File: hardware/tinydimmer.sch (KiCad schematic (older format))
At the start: 37 parts, among them J1 CTB7000/6, J2 CTB7000/2, Q1 IRL540N, SW1 SW_Push, T1 Hahn EL 305 2051, U1 BAJ0CC0T, U2 Digispark USB, U3 Busch_Dimmer_2112U_101

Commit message: Adjust pads, rewire connectors, change footprints
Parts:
- added H5: MountingHole_Pad, MountingHole:MountingHole_3.2mm_M3_Pad, symbol Mechanical:MountingHole_Pad
- D5: footprint Diode_THT:D_DO-35_SOD27_P7.62mm_Horizontal -> Diode_THT:D_DO-35_SOD27_P3.81mm_Vertical_AnodeUp
- R2, R3: footprint Resistor_THT:R_Axial_DIN0207_L6.3mm_D2.5mm_P10.16mm_Horizontal -> Resistor_THT:R_Axial_DIN0207_L6.3mm_D2.5mm_P5.08mm_Vertical
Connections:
- net GND: now also J1.3 (Pin_3), H5.1; no longer J1.5 (Pin_5)
- net PWM: now also R2.1; no longer R2.2
- net SW_NEG: now also J1.5 (Pin_5); no longer J1.1 (Pin_1)
- net SW_POS: now also J1.1 (Pin_1); no longer J1.3 (Pin_3)
- net at Q1.1 (G), R3.1: now also R2.2; no longer R2.1
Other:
- note added: "Load ground"
- note added: "Load positive"
- note added: "Potentiometer negative"
- note added: "Potentiometer positive"
- note added: "Supply ground"
- note added: "Supply positive"
- note removed: "To LED PSU"
- note removed: "To LEDs"
- note removed: "To potentiometer"
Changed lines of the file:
@@
 F 0 "R2" V 3993 4175 50  0000 C CNN
 F 1 "1K" V 4084 4175 50  0000 C CNN
-F 2 "Resistor_THT:R_Axial_DIN0207_L6.3mm_D2.5mm_P10.16mm_Horizontal" V 4130 4175 50  0001 C CNN
+F 2 "Resistor_THT:R_Axial_DIN0207_L6.3mm_D2.5mm_P5.08mm_Vertical" V 4130 4175 50  0001 C CNN
 F 3 "~" H 4200 4175 50  0001 C CNN
 	1    4200 4175
-	0    1    1    0
+	0    -1   -1   0
 $EndComp
 $Comp
@@
 F 0 "R3" H 4520 4471 50  0000 L CNN
 F 1 "10K" H 4520 4380 50  0000 L CNN
-F 2 "Resistor_THT:R_Axial_DIN0207_L6.3mm_D2.5mm_P10.16mm_Horizontal" V 4380 4425 50  0001 C CNN
+F 2 "Resistor_THT:R_Axial_DIN0207_L6.3mm_D2.5mm_P5.08mm_Vertical" V 4380 4425 50  0001 C CNN
 F 3 "~" H 4450 4425 50  0001 C CNN
 	1    4450 4425
@@
 	0    -1   -1   0
 $EndComp
-Text GLabel 9175 1400 0    50   Input ~ 0
+Text GLabel 9175 1300 0    50   Input ~ 0
 SW_POS
-Text GLabel 9175 1200 0    50   Input ~ 0
+Text GLabel 9175 1600 0    50   Input ~ 0
 SW_NEG
 Text GLabel 9175 1700 0    50   Input ~ 0
 POT_POS
 Wire Wire Line
-	9375 1500 9275 1500
-Wire Wire Line
-	9275 1500 9275 1600
-Wire Wire Line
-	9275 1600 9375 1600
-Wire Wire Line
 	9375 1400 9275 1400
 Wire Wire Line
+	9275 1400 9275 1500
+Wire Wire Line
+	9275 1500 9375 1500
+Wire Wire Line
 	9375 1300 9275 1300
 Wire Wire Line
-	9275 1300 9275 1400
-Connection ~ 9275 1400
-Wire Wire Line
-	9275 1400 9175 1400
-Wire Wire Line
-	9375 1200 9175 1200
+	9375 1200 9275 1200
+Wire Wire Line
+	9275 1200 9275 1300
+Connection ~ 9275 1300
+Wire Wire Line
+	9275 1300 9175 1300
+Wire Wire Line
+	9375 1600 9175 1600
 Wire Wire Line
 	9375 1700 9175 1700
@@
 $EndComp
 Wire Wire Line
-	9275 1850 9275 1600
-Connection ~ 9275 1600
+	9275 1850 9275 1500
+Connection ~ 9275 1500
 Wire Wire Line
 	5250 6050 5450 6050
@@
 F 0 "D5" V 4350 6150 50  0000 L CNN
 F 1 "1N5231" V 4450 6000 50  0000 L CNN
-F 2 "Diode_THT:D_DO-35_SOD27_P7.62mm_Horizontal" H 4350 6300 50  0001 C CNN
+F 2 "Diode_THT:D_DO-35_SOD27_P3.81mm_Vertical_AnodeUp" H 4350 6300 50  0001 C CNN
 F 3 "~" H 4350 6300 50  0001 C CNN
 	1    4350 6300
@@
 Wire Notes Line
 	4575 1325 4600 1325
-Text Notes 9725 1725 0    100  ~ 0
-To potentiometer
-Text Notes 9725 1525 0    100  ~ 0
-To LED PSU
-Text Notes 9725 1325 0    100  ~ 0
-To LEDs
 Wire Wire Line
 	5125 3875 4850 3875
@@
 	1    0    0    -1
 $EndComp
-Wire Wire Line
-	10175 2850 10325 2850
 $Comp
 L power:GND #PWR021
 U 1 1 5DDB9F38
-P 10325 2950
-F 0 "#PWR021" H 10325 2700 50  0001 C CNN
-F 1 "GND" H 10330 2777 50  0000 C CNN
-F 2 "" H 10325 2950 50  0001 C CNN
-F 3 "" H 10325 2950 50  0001 C CNN
-	1    10325 2950
-	1    0    0    -1
-$EndComp
-Wire Wire Line
-	10325 2950 10325 2850
-Connection ~ 10325 2850
-Wire Wire Line
-	10325 2850 10475 2850
+P 10475 3000
+F 0 "#PWR021" H 10475 2750 50  0001 C CNN
+F 1 "GND" H 10480 2827 50  0000 C CNN
+F 2 "" H 10475 3000 50  0001 C CNN
+F 3 "" H 10475 3000 50  0001 C CNN
+	1    10475 3000
+	1    0    0    -1
+$EndComp
 Wire Wire Line
 	9275 2275 9375 2275
@@
 Wire Wire Line
 	3300 1750 3300 2200
+$Comp
+L Mechanical:MountingHole_Pad H5
+U 1 1 5DD960E1
+P 10775 2750
+F 0 "H5" H 10875 2753 50  0000 L CNN
+F 1 "MountingHole_Pad" H 10875 2708 50  0001 L CNN
+F 2 "MountingHole:MountingHole_3.2mm_M3_Pad" H 10775 2750 50  0001 C CNN
+F 3 "~" H 10775 2750 50  0001 C CNN
+	1    10775 2750
+	1    0    0    -1
+$EndComp
+Wire Wire Line
+	10475 2850 10475 2925
+Wire Wire Line
+	10775 2850 10775 2925
+Connection ~ 10475 2925
+Wire Wire Line
+	10475 2925 10775 2925
+Wire Wire Line
+	10475 2925 10475 3000
+Text Notes 9700 1750 0    50   ~ 0
+Potentiometer positive
+Text Notes 9700 1550 0    50   ~ 0
+Potentiometer negative
+Text Notes 9700 1650 0    50   ~ 0
+Load ground
+Text Notes 9700 1250 0    50   ~ 0
+Load positive
+Text Notes 9700 1450 0    50   ~ 0
+Supply ground
+Text Notes 9700 1350 0    50   ~ 0
+Supply positive
+Wire Wire Line
+	10175 2850 10175 2925
+Wire Wire Line
+	10175 2925 10475 2925
 $EndSCHEMATC

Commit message: First PCB draft
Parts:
- D5: footprint Diode_THT:D_DO-35_SOD27_P3.81mm_Vertical_AnodeUp -> Diode_THT:D_DO-35_SOD27_P7.62mm_Horizontal
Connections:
- net ENABLE: now also C5.1
- net at D5.1 (K), R6.1, R7.2: no longer C5.1
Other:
- moved on the sheet: C5, R7, R8
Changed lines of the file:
@@
 	5250 6150 5250 6050
 Wire Wire Line
-	5100 6050 5250 6050
-Connection ~ 4650 6550
+	4775 6050 4925 6050
 Wire Wire Line
 	5250 6550 5250 6450
-Wire Wire Line
-	4650 6550 5250 6550
 $Comp
 L Device:R R8
 U 1 1 5DCDCA32
-P 5250 6300
-F 0 "R8" H 5100 6250 50  0000 C CNN
-F 1 "10K" H 5100 6350 50  0000 C CNN
-F 2 "Resistor_THT:R_Axial_DIN0207_L6.3mm_D2.5mm_P10.16mm_Horizontal" V 5180 6300 50  0001 C CNN
-F 3 "~" H 5250 6300 50  0001 C CNN
-	1    5250 6300
+P 4925 6300
+F 0 "R8" H 5050 6250 50  0000 C CNN
+F 1 "10K" H 5075 6350 50  0000 C CNN
+F 2 "Resistor_THT:R_Axial_DIN0207_L6.3mm_D2.5mm_P10.16mm_Horizontal" V 4855 6300 50  0001 C CNN
+F 3 "~" H 4925 6300 50  0001 C CNN
+	1    4925 6300
 	-1   0    0    1
 $EndComp
@@
 L Device:R R7
 U 1 1 5DCE45AA
-P 4950 6050
-F 0 "R7" V 4743 6050 50  0000 C CNN
-F 1 "1K" V 4834 6050 50  0000 C CNN
-F 2 "Resistor_THT:R_Axial_DIN0207_L6.3mm_D2.5mm_P10.16mm_Horizontal" V 4880 6050 50  0001 C CNN
-F 3 "~" H 4950 6050 50  0001 C CNN
-	1    4950 6050
+P 4625 6050
+F 0 "R7" V 4418 6050 50  0000 C CNN
+F 1 "1K" V 4509 6050 50  0000 C CNN
+F 2 "Resistor_THT:R_Axial_DIN0207_L6.3mm_D2.5mm_P10.16mm_Horizontal" V 4555 6050 50  0001 C CNN
+F 3 "~" H 4625 6050 50  0001 C CNN
+	1    4625 6050
 	0    1    1    0
 $EndComp
@@
 F 0 "D5" V 4350 6150 50  0000 L CNN
 F 1 "1N5231" V 4450 6000 50  0000 L CNN
-F 2 "Diode_THT:D_DO-35_SOD27_P3.81mm_Vertical_AnodeUp" H 4350 6300 50  0001 C CNN
+F 2 "Diode_THT:D_DO-35_SOD27_P7.62mm_Horizontal" H 4350 6300 50  0001 C CNN
 F 3 "~" H 4350 6300 50  0001 C CNN
 	1    4350 6300
@@
 Wire Wire Line
 	4350 6150 4350 6050
-Connection ~ 4350 6050
-Wire Wire Line
-	4350 6050 4650 6050
 Wire Wire Line
 	3800 6050 3950 6050
@@
 L Device:C C5
 U 1 1 5DCF0DB2
-P 4650 6300
-F 0 "C5" H 4765 6346 50  0000 L CNN
-F 1 "0.1uF 25V" H 4450 6200 50  0000 L CNN
-F 2 "custom-parts:C_Disc_D6.0mm_W2.0mm_P3.81mm" H 4688 6150 50  0001 C CNN
-F 3 "~" H 4650 6300 50  0001 C CNN
-	1    4650 6300
-	1    0    0    -1
-$EndComp
-Wire Wire Line
-	4650 6150 4650 6050
-Connection ~ 4650 6050
-Wire Wire Line
-	4650 6050 4800 6050
-Wire Wire Line
-	4650 6450 4650 6550
-Wire Wire Line
-	4650 6550 4350 6550
+P 5250 6300
+F 0 "C5" H 5365 6346 50  0000 L CNN
+F 1 "0.1uF 25V" H 5050 6200 50  0000 L CNN
+F 2 "custom-parts:C_Disc_D6.0mm_W2.0mm_P3.81mm" H 5288 6150 50  0001 C CNN
+F 3 "~" H 5250 6300 50  0001 C CNN
+	1    5250 6300
+	1    0    0    -1
+$EndComp
 Wire Wire Line
 	4350 6550 4350 6650
@@
 Wire Wire Line
 	10175 2925 10475 2925
+Wire Wire Line
+	4475 6050 4350 6050
+Connection ~ 4350 6050
+Wire Wire Line
+	4350 6550 4925 6550
+Wire Wire Line
+	4925 6550 4925 6450
+Connection ~ 4925 6550
+Wire Wire Line
+	4925 6550 5250 6550
+Wire Wire Line
+	4925 6150 4925 6050
+Connection ~ 4925 6050
+Wire Wire Line
+	4925 6050 5250 6050
 $EndSCHEMATC

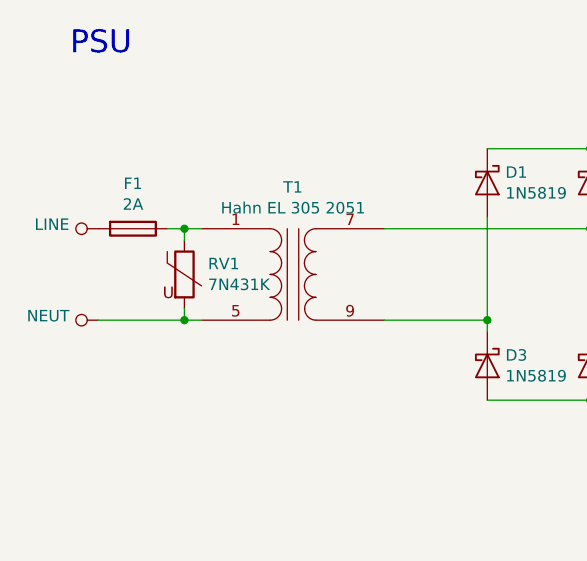
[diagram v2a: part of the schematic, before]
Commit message: Replace plain MOV with a protected GMOV
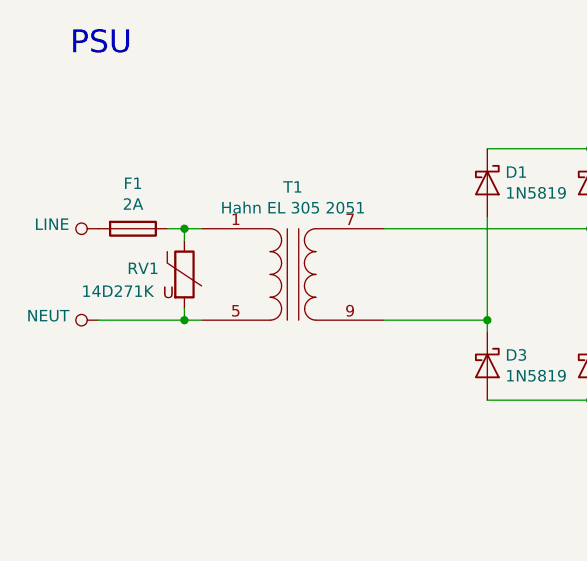
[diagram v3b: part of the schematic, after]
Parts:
- RV1: value 7N431K -> 14D271K; footprint Varistor:RV_Disc_D7mm_W3.9mm_P5mm -> Varistor:RV_Disc_D15.5mm_W3.9mm_P7.5mm
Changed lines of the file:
@@
 U 1 1 5DFDC009
 P 1525 1950
-F 0 "RV1" H 1628 1996 50  0000 L CNN
-F 1 "7N431K" H 1628 1905 50  0000 L CNN
-F 2 "Varistor:RV_Disc_D7mm_W3.9mm_P5mm" V 1455 1950 50  0001 C CNN
+F 0 "RV1" H 1275 1975 50  0000 L CNN
+F 1 "14D271K" H 1075 1875 50  0000 L CNN
+F 2 "Varistor:RV_Disc_D15.5mm_W3.9mm_P7.5mm" V 1455 1950 50  0001 C CNN
 F 3 "~" H 1525 1950 50  0001 C CNN
 	1    1525 1950
